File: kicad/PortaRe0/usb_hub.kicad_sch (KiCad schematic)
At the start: 59 parts, among them U4 VL812, U5 W25Q32JVSSIQ, Y1 25MHz

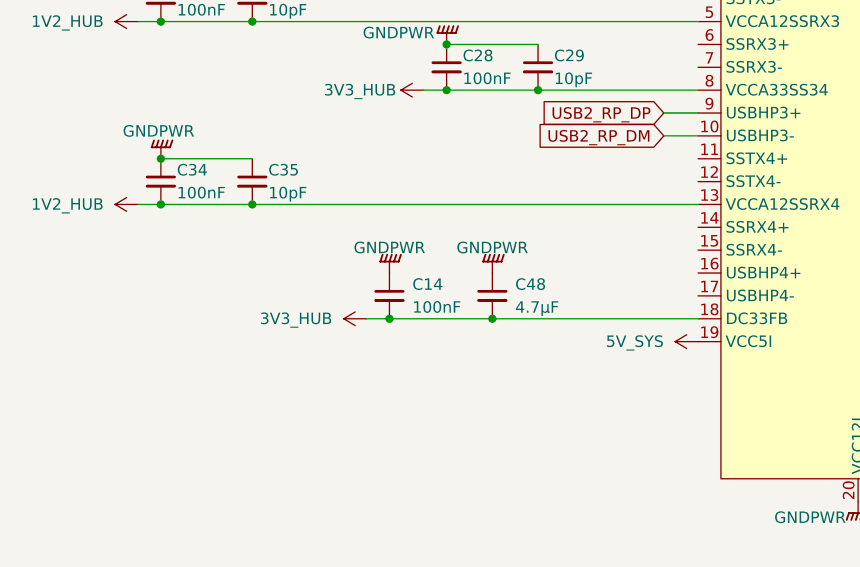
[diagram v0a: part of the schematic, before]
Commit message: session10: audio sheet完成、USB命名規則統一、TESTEN修正
- audio.kicad_sch: RP2040 #2追加、MAX98357A×2、PCM5102APWR、TPA6132A2RTER配線完了
- PCM5102APWR/TPA6132A2RTERシンボル・フットプリント追加
- I2S共有バス(BCLK/LRCLK/SDIN)でスピーカー・イヤホン共通接続
- GPIO割り当て: GP0-2=I2S, GP3=SD_MODE, GP4=XSMT, GP5=HP_EN, GP6=HP_DET
- USB命名規則統一: RP2040 #1→USB2_RP_DP/DM, RP2040 #2→USB2_RP_DP2/DM2
- VL812 USBHP4にUSB2_RP_DP2/DM2追加
- RP2040 #1/#2のTESTEN→GND修正
- BQ25895 D+/D-はUSB_DP/DM(充電用USB-C)で確定

Co-Authored-By: Claude Sonnet 4.6 <noreply@anthropic.com>
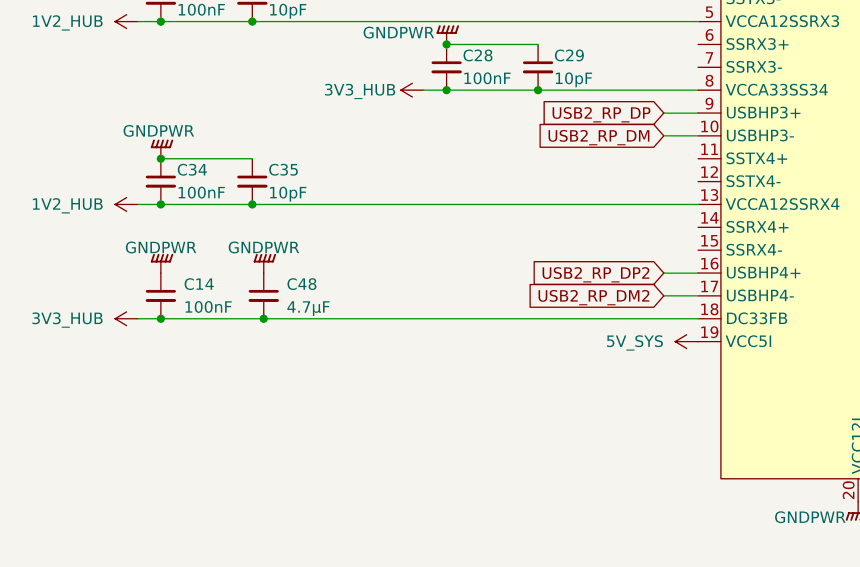
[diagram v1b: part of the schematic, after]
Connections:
- net USB2_RP_DP2: now reaches U4.16 (USBHP4+)
- net USB2_RP_DM2: now reaches U4.17 (USBHP4-)
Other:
- moved on the sheet: C14, C48
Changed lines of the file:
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@@
 	)
 	(junction
-		(at 72.39 175.26)
+		(at 46.99 175.26)
 		(diameter 0)
 		(color 0 0 0 0)
@@
 	)
 	(junction
-		(at 60.96 175.26)
+		(at 35.56 175.26)
 		(diameter 0)
 		(color 0 0 0 0)
@@
 	(wire
 		(pts
-			(xy 72.39 175.26) (xy 95.25 175.26)
+			(xy 46.99 175.26) (xy 95.25 175.26)
 		)
 		(stroke
@@
 	(wire
 		(pts
+			(xy 91.44 172.72) (xy 95.25 172.72)
+		)
+		(stroke
+			(width 0)
+			(type default)
+		)
+	)
+	(wire
+		(pts
 			(xy 157.48 201.93) (xy 156.21 201.93)
 		)
@@
 	(wire
 		(pts
+			(xy 91.44 170.18) (xy 95.25 170.18)
+		)
+		(stroke
+			(width 0)
+			(type default)
+		)
+	)
+	(wire
+		(pts
 			(xy 143.51 109.22) (xy 143.51 114.3)
 		)
@@
 	(wire
 		(pts
-			(xy 60.96 175.26) (xy 72.39 175.26)
+			(xy 35.56 175.26) (xy 46.99 175.26)
 		)
 		(stroke
@@
 	(wire
 		(pts
-			(xy 58.42 175.26) (xy 60.96 175.26)
+			(xy 33.02 175.26) (xy 35.56 175.26)
 		)
 		(stroke
@@
 		)
 	)
+	(global_label "USB2_RP_DP2"
+		(shape input)
+		(at 91.44 170.18 180)
+		(fields_autoplaced yes)
+		(effects
+			(font
+				(size 1.27 1.27)
+			)
+			(justify right)
+		)
+		(property "Intersheetrefs" "${INTERSHEET_REFS}"
+			(at 75.2106 170.18 0)
+			(effects
+				(font
+					(size 1.27 1.27)
+				)
+				(justify right)
+				(hide yes)
+			)
+		)
+	)
 	(global_label "USB2_UP_DM"
 		(shape input)
@@
 		)
 	)
+	(global_label "USB2_RP_DM2"
+		(shape input)
+		(at 91.44 172.72 180)
+		(fields_autoplaced yes)
+		(effects
+			(font
+				(size 1.27 1.27)
+			)
+			(justify right)
+		)
+		(property "Intersheetrefs" "${INTERSHEET_REFS}"
+			(at 75.0292 172.72 0)
+			(effects
+				(font
+					(size 1.27 1.27)
+				)
+				(justify right)
+				(hide yes)
+			)
+		)
+	)
 	(symbol
 		(lib_id "Device:Crystal_Small")
@@
 	(symbol
 		(lib_id "power:3V3_HUB")
-		(at 58.42 175.26 90)
+		(at 33.02 175.26 90)
 		(unit 1)
 		(exclude_from_sim no)
@@
 		(fields_autoplaced yes)
 		(property "Reference" "#PWR043"
-			(at 62.23 175.26 0)
+			(at 36.83 175.26 0)
 			(effects
 				(font
@@
 		)
 		(property "Value" "3V3_HUB"
-			(at 54.61 175.2599 90)
+			(at 29.21 175.2599 90)
 			(effects
 				(font
@@
 		)
 		(property "Footprint" ""
-			(at 58.42 175.26 0)
+			(at 33.02 175.26 0)
 			(effects
 				(font
@@
 		)
 		(property "Datasheet" ""
-			(at 58.42 175.26 0)
+			(at 33.02 175.26 0)
 			(effects
 				(font
@@
 		)
 		(property "Description" "Power symbol creates a global label with name \"VSYS\""
-			(at 52.324 175.514 0)
+			(at 26.924 175.514 0)
 			(effects
 				(font
@@
 	(symbol
 		(lib_id "Device:C_Small")
-		(at 60.96 172.72 0)
+		(at 35.56 172.72 0)
 		(unit 1)
 		(exclude_from_sim no)
@@
 		(fields_autoplaced yes)
 		(property "Reference" "C14"
-			(at 63.5 171.4562 0)
+			(at 38.1 171.4562 0)
 			(effects
 				(font
@@
 		)
 		(property "Value" "100nF"
-			(at 63.5 173.9962 0)
+			(at 38.1 173.9962 0)
 			(effects
 				(font
@@
 		)
 		(property "Footprint" ""
-			(at 60.96 172.72 0)
+			(at 35.56 172.72 0)
 			(effects
 				(font
@@
 		)
 		(property "Datasheet" "~"
-			(at 60.96 172.72 0)
+			(at 35.56 172.72 0)
 			(effects
 				(font
@@
 		)
 		(property "Description" "Unpolarized capacitor, small symbol"
-			(at 60.96 172.72 0)
+			(at 35.56 172.72 0)
 			(effects
 				(font
@@
 	(symbol
 		(lib_id "power:GNDPWR")
-		(at 72.39 170.18 180)
+		(at 46.99 170.18 180)
 		(unit 1)
 		(exclude_from_sim no)
@@
 		(dnp no)
 		(property "Reference" "#PWR0103"
-			(at 72.39 165.1 0)
+			(at 46.99 165.1 0)
 			(effects
 				(font
@@
 		)
 		(property "Value" "GNDPWR"
-			(at 72.39 167.386 0)
+			(at 46.99 167.386 0)
 			(effects
 				(font
@@
 		)
 		(property "Footprint" ""
-			(at 72.39 168.91 0)
+			(at 46.99 168.91 0)
 			(effects
 				(font
@@
 		)
 		(property "Datasheet" ""
-			(at 72.39 168.91 0)
+			(at 46.99 168.91 0)
 			(effects
 				(font
@@
 		)
 		(property "Description" "Power symbol creates a global label with name \"GNDPWR\" , global ground"
-			(at 72.39 170.18 0)
+			(at 46.99 170.18 0)
 			(effects
 				(font
@@
 	(symbol
 		(lib_id "power:GNDPWR")
-		(at 60.96 170.18 180)
+		(at 35.56 170.18 180)
 		(unit 1)
 		(exclude_from_sim no)
@@
 		(dnp no)
 		(property "Reference" "#PWR045"
-			(at 60.96 165.1 0)
+			(at 35.56 165.1 0)
 			(effects
 				(font
@@
 		)
 		(property "Value" "GNDPWR"
-			(at 60.96 167.386 0)
+			(at 35.56 167.386 0)
 			(effects
 				(font
@@
 		)
 		(property "Footprint" ""
-			(at 60.96 168.91 0)
+			(at 35.56 168.91 0)
 			(effects
 				(font
@@
 		)
 		(property "Datasheet" ""
-			(at 60.96 168.91 0)
+			(at 35.56 168.91 0)
 			(effects
 				(font
@@
 		)
 		(property "Description" "Power symbol creates a global label with name \"GNDPWR\" , global ground"
-			(at 60.96 170.18 0)
+			(at 35.56 170.18 0)
 			(effects
 				(font
@@
 	(symbol
 		(lib_id "Device:C_Small")
-		(at 72.39 172.72 0)
+		(at 46.99 172.72 0)
 		(unit 1)
 		(exclude_from_sim no)
@@
 		(fields_autoplaced yes)
 		(property "Reference" "C48"
-			(at 74.93 171.4562 0)
+			(at 49.53 171.4562 0)
 			(effects
 				(font
@@
 		)
 		(property "Value" "4.7μF"
-			(at 74.93 173.9962 0)
+			(at 49.53 173.9962 0)
 			(effects
 				(font
@@
 		)
 		(property "Footprint" ""
-			(at 72.39 172.72 0)
+			(at 46.99 172.72 0)
 			(effects
 				(font
@@
 		)
 		(property "Datasheet" "~"
-			(at 72.39 172.72 0)
+			(at 46.99 172.72 0)
 			(effects
 				(font
@@
 		)
 		(property "Description" "Unpolarized capacitor, small symbol"
-			(at 72.39 172.72 0)
+			(at 46.99 172.72 0)
 			(effects
 				(font

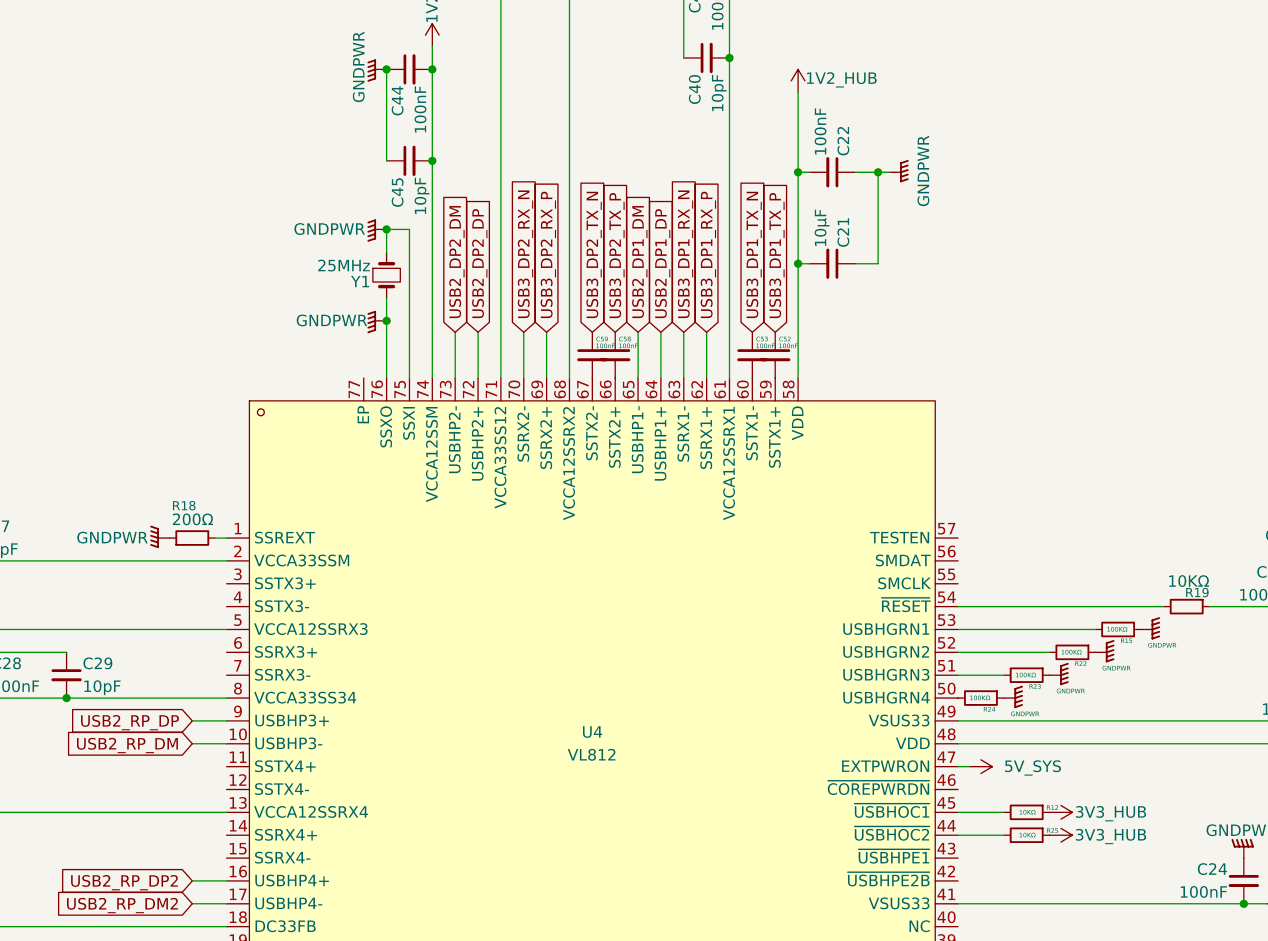
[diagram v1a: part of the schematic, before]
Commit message: Save: usb_hub.kicad_sch中間保存
Co-Authored-By: Claude Sonnet 4.6 <noreply@anthropic.com>
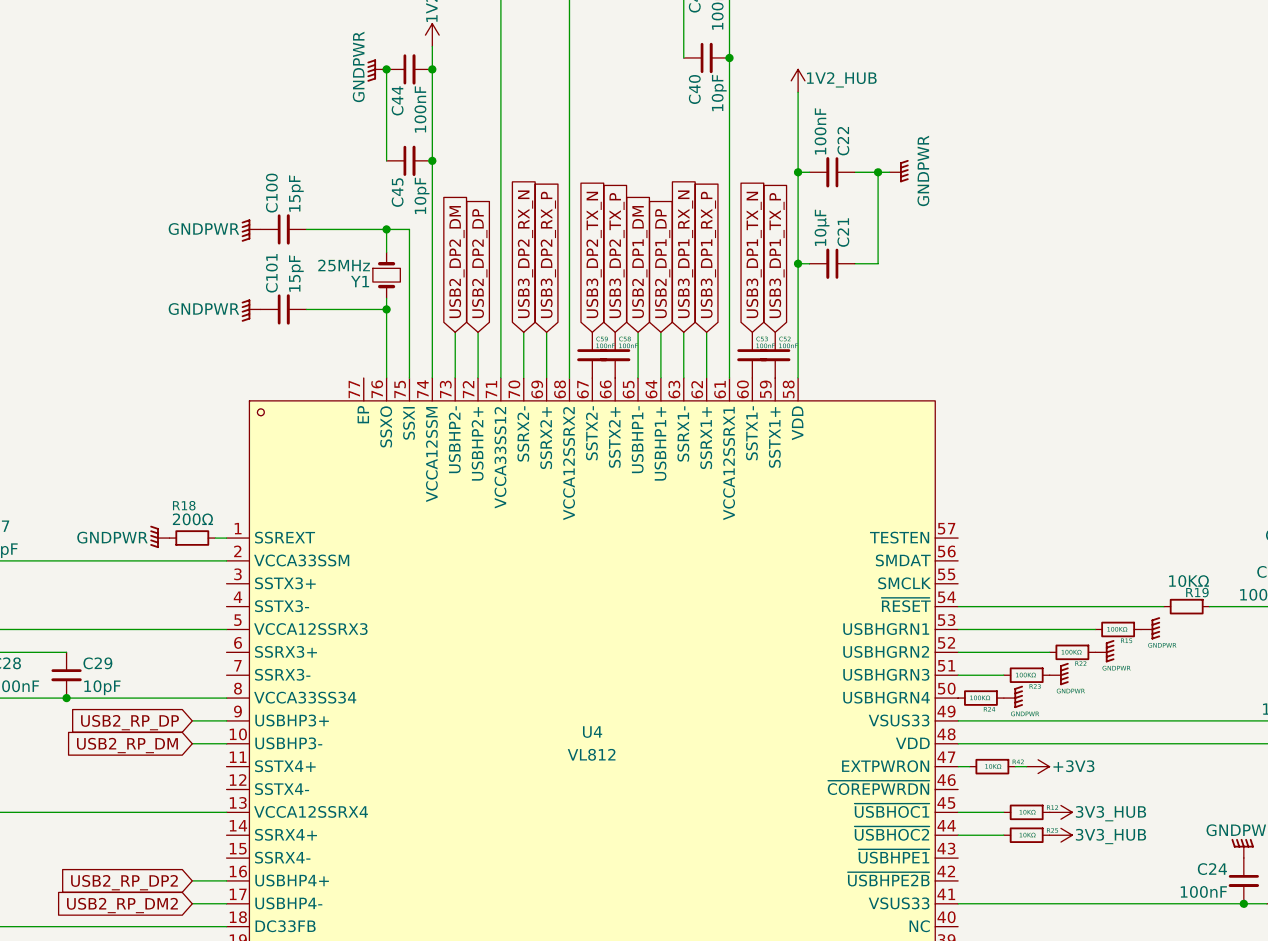
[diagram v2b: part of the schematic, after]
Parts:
- added C100, C101: 15pF, symbol Device:C_Small
- added R42: 10KΩ, symbol Device:R_Small
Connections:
- net 5V_SYS: no longer U4.47 (EXTPWRON)
- net GNDPWR: now also C100.1, C101.1; no longer U4.75 (SSXI), U4.76 (SSXO), Y1.1, Y1.2
- new net: C100.2, U4.75 (SSXI), Y1.1
- new net: C101.2, U4.76 (SSXO), Y1.2
- new net: R42.2, U4.47 (EXTPWRON)
- new net +3V3: R42.1

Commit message: usb_hub: TPS2042BDR/USBLC6-2SC6/VBUSDET/EXTPWRON実装
- TPS2042BDR配置・配線（/USBHPE1/2B、/USBHOC1/2接続）
- TPS61023 #2追加（HUB_5V生成 / EN=USB_VBUS_EN）
- USBLC6-2SC6 × 2配置（Port1=USB-C / Port2=USB-A）
- VL812 VBUSDET: 56kΩ+100kΩ分圧（USB2_UP_VBUSから）
- VL812 EXTPWRON: 10kΩ→3V3_HUBプルアップに変更
- Net Label命名: HUB_USBC_DP/DM / HUB_USBA_DP/DM
- VL812水晶負荷コンデンサC44/C45 = 18pF設定
- Port1/2割り当て修正（Port1=USB-C / Port2=USB-A）
- Docs: Claude.md/PROGRESS.md更新

Co-Authored-By: Claude Sonnet 4.6 <noreply@anthropic.com>
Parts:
- removed R13, R14, R21: 100KΩ, symbol Device:R_Small
- added C102: 10µF, symbol Device:C_Small
- added C103, C105, C106: 100nF, symbol Device:C_Small
- added C104: 22µF, symbol Device:C_Small
- added C107, C108: 150μF, symbol Device:C_Small
- added D5: USB_HUB_C, PortaRe0:SOT-23-6_L2.9-W1.6-P0.95-LS2.8-BL, symbol PortaRe0:USBLC6-2SC6
- added D6: USB_HUB_A, PortaRe0:SOT-23-6_L2.9-W1.6-P0.95-LS2.8-BL, symbol PortaRe0:USBLC6-2SC6
- added L4: 1µH / 3A, symbol Device:L_Small
- added R43, R44: 100kΩ, symbol Device:R_Small
- added R45: 910kΩ, symbol Device:R_Small
- added R46: 56KΩ, symbol Device:R_Small
- added R47: 100KΩ, symbol Device:R_Small
- added SW3: SW_START, symbol Switch:SW_SPST
- added SW4: KillSW, symbol Switch:SW_SPDT
- added U10: TPS2042BDR, PortaRe0:SOIC-8_L4.9-W3.9-P1.27-LS6.0-BL, symbol PortaRe0:TPS2042BDR
- added U7: TPS61023DRLR, PortaRe0:SOT-563_L1.6-W1.2-P0.50-LS1.6-BR, symbol PortaRe0:TPS61023DRLR
- C100, C101: value 15pF -> 18pF
- R18: value 200Ω -> 12.1kΩ
- R20: value 100KΩ -> 10KΩ
- renumbered Y1 to C9006
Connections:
- net 5V_SYS: now also R45.1; no longer U4.31 (VBUSDET)
- net GNDPWR: now also C102.2, C103.2, C104.1, C105.1, C106.2, C107.2, C108.2, D5.2, D6.2, R43.2, R44.1, R47.1, U10.1 (GND), U7.4 (GND)
- net USB2_DP1_DM: now also D5.3
- net USB2_DP1_DP: now also D5.1
- net USB2_DP2_DM: now also D6.3
- net USB2_DP2_DP: now also D6.1
- net USBHOC2: now reaches R25.2, U4.44 (~{USBHOC2})
- net USBHOC2: now also U10.5 (~{OC2})
- net USBHOC1: now reaches R12.2, U4.45 (~{USBHOC1})
- net USBHOC1: now also U10.8 (~{OC1})
- net USBHPE2: now reaches U4.42 (~{USBHPE2B})
- net USBHPE2: now also U10.4 (~{EN2})
- net USBHPE1: now reaches U4.43 (~{USBHPE1})
- net USBHPE1: now also U10.3 (~{EN1})
- new net: R44.2, R45.2, U7.1 (FB)
- new net: SW4.1 (A), U7.3 (VIN)
- new net: L4.1, U7.5 (SW)
- new net: R46.2, R47.2, U4.31 (VBUSDET)
- new net HUB_5V: C104.2, C105.2, C106.1, D5.5, D6.5, U10.2 (IN), U7.6 (VOUT)
- new net HUB_USBA_DM: D6.4
- new net HUB_USBA_DP: D6.6
- new net HUB_USBC_DM: D5.4
- new net HUB_USBC_DP: D5.6
- new net USB1_VBUS: C107.1, U10.7 (OUT1)
- new net USB2_UP_VBUS: R46.1
- new net USB2_VBUS: C108.1, U10.6 (OUT2)
- new net USB_VBUS_EN: R43.1, SW3.2 (B), U7.2 (EN)
- new net VSYS: C102.1, C103.1, L4.2, SW3.1 (A), SW4.2 (B)
- no-connect marks 0 -> 1
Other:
- moved on the sheet: C24, C66, R12, R16, R17, R20, R25, U5

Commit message: Docs: session18終了処理・PROGRESS/index更新・connectorsシート設計方針確定
- J_HDMI_CTRL: 24pin FPC 0.5mm (C2856805) ライブラリ取得・配置方針確定
- SBC接続: サブ基板→FPCに変更・スティフナーにMicro HDMIオス+USB-Cオス直付け方針
- connectors.kicad_sch 追加

Co-Authored-By: Claude Sonnet 4.6 <noreply@anthropic.com>
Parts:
- removed C9006: 25MHz, symbol Device:Crystal_Small
- added R13: 100KΩ, symbol Device:R_Small
- added R50, R51: 56kΩ, symbol Device:R_Small
- added U12: HC-USB3.0-L168-WP, PortaRe0:USB-TH_USB3.0-A, symbol PortaRe0:HC-USB3.0-L168-WP
- added U8: USB31-TYPE-C-FSABC, PortaRe0:USB-C-SMD_USB31-TYPE-C-FSABC, symbol PortaRe0:USB31-TYPE-C-FSABC
- added Y1: C9006, symbol Device:Crystal_GND24_Small
- C67: value 100nF -> 1μF
- L3: value 4.7μH -> 10μH
- R18: value 12.1kΩ -> 6.04kΩ
- R46: value 56KΩ -> 4.7KΩ
- R47: value 100KΩ -> 10KΩ
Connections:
- net +3V3 is gone; now on net 3V3_HUB: R42.1
- net 3V3_HUB: now also R13.1
- net GNDPWR: now also R13.2, U12.10 (SH), U12.4 (GND), U12.7 (GND_DRAN), U8.25 (EH), U8.26 (EH), U8.27 (EH), U8.28 (EH), U8.A1 (GND), U8.A12 (GND), U8.B1 (GND), U8.B12 (GND), Y1.2, Y1.4
- net HUB_5V: now also R50.2, R51.1, U12.1 (VBUS), U8.A4 (VBUS), U8.A9 (VBUS), U8.B4 (VBUS), U8.B9 (VBUS)
- net HUB_USBA_DM: now also U12.2 (D-)
- net HUB_USBA_DP: now also U12.3 (D+)
- net HUB_USBC_DM: now also U8.A7 (DN1), U8.B7 (DN2)
- net HUB_USBC_DP: now also U8.A6 (DP1), U8.B6 (DP2)
- net USB3_DP1_RX_N: now also U8.A10 (SSRXn2), U8.B10 (SSRXn1)
- net USB3_DP1_RX_P: now also U8.A11 (SSRXp2), U8.B11 (SSRXp1)
- net USB3_DP1_TX_N: now also U8.A3 (SSTXn1), U8.B3 (SSTXn2)
- net USB3_DP1_TX_P: now also U8.A2 (SSTXP1), U8.B2 (SSTXp2)
- net USB3_DP2_RX_N: now also U12.5 (SSRX-)
- net USB3_DP2_RX_P: now also U12.6 (SSRX+)
- net USB3_DP2_TX_N: now also U12.8 (SSTX-)
- net USB3_DP2_TX_P: now also U12.9 (SSTX+)
- net at C100.2, U4.75 (SSXI): now also Y1.1
- net at C101.2, U4.76 (SSXO): now also Y1.3
- new net: R50.1, U8.A5 (CC1)
- new net: R51.2, U8.B5 (CC2)
- no-connect marks 1 -> 3
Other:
- moved on the sheet: C66, R16, R17, R20, U5

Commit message: KiCad: connectorsシート更新（J_HDMI_CTRL・J_SBC_USB1・J_SBC_USB2配置・配線）
Co-Authored-By: Claude Sonnet 4.6 <noreply@anthropic.com>
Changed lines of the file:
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@@
-		)
-	)
-	(label "USB2_UP_VBUS"
-		(at 140.97 223.52 270)
-		(effects
-			(font
-				(size 1.27 1.27)
-			)
-			(justify right bottom)
 		)
 	)
@@
 			(effects
 				(font
+					(size 1.27 1.27)
+				)
+				(justify right)
+				(hide yes)
+			)
+		)
+	)
+	(global_label "USB2_UP_VBUS"
+		(shape input)
+		(at 140.97 223.52 270)
+		(fields_autoplaced yes)
+		(effects
+			(font
+				(size 1.27 1.27)
+			)
+			(justify right)
+		)
+		(property "Intersheetrefs" "${INTERSHEET_REFS}"
+			(at 140.97 240.959 90)
+			(effects
+				(font

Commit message: Docs: session21終了処理・PROGRESS/index更新・connectorsシート完成・ERC対処
- connectors シート完成（J_SBC_HDMI / J_FAN配置完了）
- hdmi_adapter シート新設（別基板 / J_MICROHDMI Conn_02x08 + C2856805）
- J_FAN: F16FB選定（16×16×4.5mm 5V）/ BSS138回路 / FAN_PWM GlobalLabel
- 全シートERC実施・対処完了（VL812未接続ピン / SWD NC / DC10FB追加等）

Co-Authored-By: Claude Sonnet 4.6 <noreply@anthropic.com>
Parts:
- added C111: 10μF, symbol Device:C_Small
- added C112: 100nF, symbol Device:C_Small
- added R58, R59: 4.7KΩ, symbol Device:R_Small
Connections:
- net 1V2_HUB: now also U4.21 (DC10FB), C111.2, C112.2
- net 3V3_HUB: now also R58.1, R59.1
- net GNDPWR: now also U4.46 (~{COREPWRDN}), U4.57 (TESTEN), U4.77 (EP), C111.1, C112.1
- net at U4.55 (SMCLK): now also R59.2
- net at U4.56 (SMDAT): now also R58.2
- no-connect marks 3 -> 12

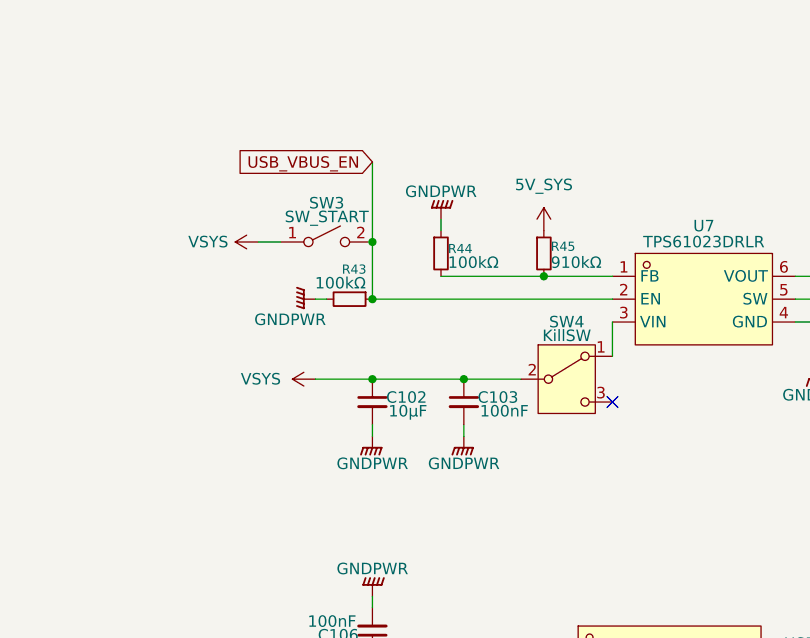
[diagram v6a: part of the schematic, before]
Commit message: Docs/KiCad: session24終了処理・チェックシート作成・回路修正
- Claude/checklists/ 新規作成（IC設計レビュー用 01〜10）
- BQ25895修正: C5(4.7nF→4.7µF) / CE(3V3→GND) / QON(GND→NC)
- TPS61023修正: R_TOP(910kΩ→750kΩ, 5.1V) / SW2をVSYS直列に変更 / usb_hub SW4削除
- AP2112K: バイパスキャップ1µF→10µF
- PROGRESS.md・index.md更新

Co-Authored-By: Claude Sonnet 4.6 <noreply@anthropic.com>
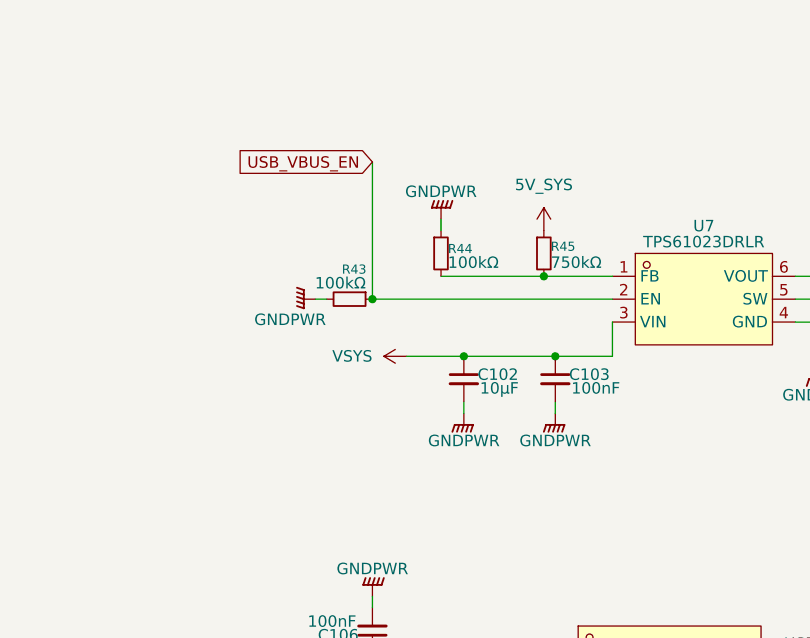
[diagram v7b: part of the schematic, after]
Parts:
- removed SW3: SW_START, symbol Switch:SW_SPST
- removed SW4: KillSW, symbol Switch:SW_SPDT
- R45: value 910kΩ -> 750kΩ
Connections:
- net VSYS: now also U7.3 (VIN)
- no-connect marks 12 -> 11
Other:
- moved on the sheet: C102, C103
